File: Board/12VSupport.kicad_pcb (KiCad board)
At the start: 2 copper layers, 106.7 x 123.2 mm, 86 parts, among them J1 12V, J2 BATT, J3 BUCK_IN, J4 BUCK_OUT, J5 BOOST_IN, J6 BOOST_OUT, J7 TMP36GZ, J8 HEATER, J9 ICSP, K1 SLA-05VDC-SL-C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

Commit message: Minor improvements
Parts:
- added C10: 100n, Capacitor_SMD:C_0805_2012Metric, F.Cu at (76.2, 50.8)
- U2: value PIC18F2480 -> PIC18F2480-ISO
- moved R23 2.37 mm to (131.8, 114.7)
- moved L3 0.40 mm to (130.2, 110.1)
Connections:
- F1 pad 2: Net-(F1-Pad2) -> B-
- K1 pad 11A: Net-(F1-Pad2) -> B-
- K1 pad 11B: Net-(F1-Pad2) -> B-
- K2 pad 11A: Net-(K2-Pad11A) -> B+
- K2 pad 11B: Net-(K2-Pad11A) -> B+
- R17 pad 1: BUCK+ -> B+
- R8 pad 1: BUCK- -> B-
- U4 pad 3: Net-(K2-Pad11A) -> B+
- U4 pad 4: Net-(K2-Pad11A) -> B+
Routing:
- net B+: track 0.00 -> 136.3 mm, vias 0 -> 6
- net Net-(K2-Pad11A): track 112.5 -> 0.00 mm, vias 6 -> 0
- net BUCK+: track 166.2 -> 74.9 mm, vias 2 -> 1
- net B-: track 0.00 -> 70.1 mm
- net Net-(F1-Pad2): track 58.3 -> 0.00 mm
- net BUCK-: track 109.5 -> 52.3 mm, vias 1 -> 0
- net GND: track 493.5 -> 439.1 mm, vias 53 -> 50
- net CURR_SENSE: track 135.0 -> 131.7 mm, vias 4 -> 2
- net Net-(J1-Pin_2): track 18.4 -> 16.2 mm
- net VCC: track 317.0 -> 315.1 mm
- net /MCU/VPP: track 21.6 -> 19.7 mm
- net Net-(J7-Pin_2): track 61.4 -> 62.5 mm
- net Net-(U5A--): track 21.4 -> 20.5 mm
- net REL_HEATER: track 158.4 -> 159.2 mm
- net /MCU/VCC_PIC: track 50.5 -> 49.6 mm
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
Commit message: Rev. 1.1
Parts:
- moved J8 0.47 mm to (48.5, 77.6)
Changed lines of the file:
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@@
 	(footprint "TerminalBlock:TerminalBlock_Altech_AK300-2_P5.00mm"
 		(layer "F.Cu")
-		(at 48.4105 77.136 90)
+		(at 48.514 77.597 90)
 		(descr "Altech AK300 terminal block, pitch 5.0mm, 45 degree angled, see http://www.mouser.com/ds/2/16/PCBMETRC-24178.pdf")
 		(tags "Altech AK300 terminal block pitch 5.0mm")
@@
 	)
 	(segment
-		(start 58.674 67.564)
-		(end 54.102 72.136)
-		(width 1.2)
+		(start 101.098167 49.917167)
+		(end 104.919 53.738)
+		(width 0.4)
 		(layer "F.Cu")
 		(net 3)
 	)
 	(segment
-		(start 101.098167 49.917167)
-		(end 104.919 53.738)
-		(width 0.4)
+		(start 104.14 67.564)
+		(end 58.674 67.564)
+		(width 1.2)
 		(layer "F.Cu")
 		(net 3)
@@
 	)
 	(segment
+		(start 106.172 69.596)
+		(end 104.14 67.564)
+		(width 1.2)
+		(layer "F.Cu")
+		(net 3)
+	)
+	(segment
+		(start 48.975 72.136)
+		(end 48.514 72.597)
+		(width 1.2)
+		(layer "F.Cu")
+		(net 3)
+	)
+	(segment
 		(start 131.185 65.193)
 		(end 126.493 65.193)
@@
 	)
 	(segment
+		(start 58.674 67.564)
+		(end 54.102 72.136)
+		(width 1.2)
+		(layer "F.Cu")
+		(net 3)
+	)
+	(segment
 		(start 93.726 54.864)
 		(end 95.28 56.418)
@@
 	)
 	(segment
+		(start 54.102 72.136)
+		(end 48.975 72.136)
+		(width 1.2)
+		(layer "F.Cu")
+		(net 3)
+	)
+	(segment
 		(start 104.919 53.738)
 		(end 116.078 53.738)
@@
 	)
 	(segment
-		(start 54.102 72.136)
-		(end 48.4105 72.136)
-		(width 1.2)
-		(layer "F.Cu")
-		(net 3)
-	)
-	(segment
 		(start 57.1405 113.886)
 		(end 65.118 113.886)
@@
 	)
 	(segment
-		(start 58.674 67.564)
-		(end 104.14 67.564)
-		(width 1.2)
-		(layer "F.Cu")
-		(net 3)
-	)
-	(segment
-		(start 104.14 67.564)
-		(end 106.172 69.596)
-		(width 1.2)
-		(layer "F.Cu")
-		(net 3)
-	)
-	(segment
 		(start 106.172 72.136)
 		(end 106.172 69.596)
@@
 	)
 	(segment
-		(start 61.5655 77.464)
-		(end 48.7385 77.464)
+		(start 48.647 77.464)
+		(end 48.514 77.597)
 		(width 1.2)
 		(layer "F.Cu")
@@
 	)
 	(segment
-		(start 48.7385 77.464)
-		(end 48.4105 77.136)
+		(start 61.5655 77.464)
+		(end 48.647 77.464)
 		(width 1.2)
 		(layer "F.Cu")

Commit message: Silkscreen fix
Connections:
- net Net-(J6-Pin_1) renamed /BO-
- net Net-(J6-Pin_2) renamed /BO+
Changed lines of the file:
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@@
 	(net 27 "/BUCK_OUT+")
 	(net 28 "/BOOST_IN+")
-	(net 29 "Net-(J6-Pin_1)")
-	(net 30 "Net-(J6-Pin_2)")
+	(net 29 "/BO+")
+	(net 30 "/BO-")
 	(net 31 "Net-(J8-Pin_1)")
 	(net 32 "/MCU/VPP")
@@
 			(layers "*.Cu" "*.Mask" "F.SilkS")
 			(remove_unused_layers no)
-			(net 29 "Net-(J6-Pin_1)")
+			(net 30 "/BO-")
 			(pinfunction "Pin_1")
 			(pintype "passive")
@@
 			(layers "*.Cu" "*.Mask" "F.SilkS")
 			(remove_unused_layers no)
-			(net 30 "Net-(J6-Pin_2)")
+			(net 29 "/BO+")
 			(pinfunction "Pin_2")
 			(pintype "passive")
@@
 			(layers "*.Cu" "*.Mask")
 			(remove_unused_layers no)
-			(net 30 "Net-(J6-Pin_2)")
+			(net 29 "/BO+")
 			(pintype "passive")
 		)
@@
 			(layers "*.Cu" "*.Mask")
 			(remove_unused_layers no)
-			(net 29 "Net-(J6-Pin_1)")
+			(net 30 "/BO-")
 			(pintype "passive")
 		)
@@
 	)
 	(gr_text "+"
-		(at 56.896 148.336 270)
+		(at 44.196 148.336 270)
 		(layer "F.SilkS")
 		(effects
@@
 	)
 	(gr_text "+"
-		(at 91.948 148.336 270)
+		(at 79.248 148.336 270)
 		(layer "F.SilkS")
 		(effects
@@
 	)
 	(gr_text "+"
-		(at 74.168 148.336 270)
+		(at 61.468 148.336 270)
 		(layer "F.SilkS")
 		(effects
@@
 	)
 	(gr_text "+"
-		(at 109.728 148.336 270)
+		(at 97.028 148.336 270)
 		(layer "F.SilkS")
 		(effects
@@
 	)
 	(segment
-		(start 63.945 109.304)
-		(end 63.945 122.618)
-		(width 2.4)
-		(layer "B.Cu")
-		(net 29)
-	)
-	(segment
-		(start 63.945 122.618)
-		(end 60.452 126.111)
-		(width 2.4)
-		(layer "B.Cu")
-		(net 29)
-	)
-	(segment
-		(start 60.452 126.111)
-		(end 60.452 141.288)
-		(width 2.4)
-		(layer "B.Cu")
-		(net 29)
-	)
-	(segment
-		(start 63.627 108.986)
-		(end 63.945 109.304)
-		(width 2.4)
-		(layer "B.Cu")
-		(net 29)
-	)
-	(segment
-		(start 60.452 141.288)
-		(end 72.644 153.48)
-		(width 2.4)
-		(layer "B.Cu")
-		(net 29)
-	)
-	(segment
 		(start 99.29 110.998)
 		(end 101.558 108.73)
 		(width 2.4)
 		(layer "F.Cu")
-		(net 30)
+		(net 29)
 	)
 	(segment
@@
 		(width 2.4)
 		(layer "F.Cu")
-		(net 30)
+		(net 29)
 	)
 	(segment
@@
 		(width 2.4)
 		(layer "F.Cu")
-		(net 30)
+		(net 29)
 	)
 	(segment
@@
 		(width 2.4)
 		(layer "F.Cu")
-		(net 30)
+		(net 29)
 	)
 	(segment
@@
 		(width 2.4)
 		(layer "F.Cu")
-		(net 30)
+		(net 29)
 	)
 	(via
@@
 		(drill 0.8)
 		(layers "F.Cu" "B.Cu")
-		(net 30)
+		(net 29)
 	)
 	(segment
@@
 		(width 2.4)
 		(layer "B.Cu")
-		(net 30)
+		(net 29)
 	)
 	(segment
@@
 		(width 2.4)
 		(layer "B.Cu")
-		(net 30)
+		(net 29)
 	)
 	(segment
@@
 		(width 2.4)
 		(layer "B.Cu")
-		(net 30)
+		(net 29)
 	)
 	(segment
@@
 		(width 2.4)
 		(layer "B.Cu")
+		(net 29)
+	)
+	(segment
+		(start 63.945 109.304)
+		(end 63.945 122.618)
+		(width 2.4)
+		(layer "B.Cu")
+		(net 30)
+	)
+	(segment
+		(start 63.945 122.618)
+		(end 60.452 126.111)
+		(width 2.4)
+		(layer "B.Cu")
+		(net 30)
+	)
+	(segment
+		(start 60.452 126.111)
+		(end 60.452 141.288)
+		(width 2.4)
+		(layer "B.Cu")
+		(net 30)
+	)
+	(segment
+		(start 63.627 108.986)
+		(end 63.945 109.304)
+		(width 2.4)
+		(layer "B.Cu")
+		(net 30)
+	)
+	(segment
+		(start 60.452 141.288)
+		(end 72.644 153.48)
+		(width 2.4)
+		(layer "B.Cu")

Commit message: Bugfixes
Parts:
- added R20: 33K, Resistor_SMD:R_0805_2012Metric, F.Cu at (58.2, 65.3)
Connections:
- C6 pad 1: Net-(U5C--) -> Net-(U5C-+)
- R5 pad 2: Net-(U5C--) -> Net-(U5C-+)
- R6 pad 1: Net-(U5C--) -> Net-(U5C-+)
- U5 pad 10: 12V_SENSE -> Net-(U5C-+)
- U5 pad 9: Net-(U5C--) -> 12V_SENSE
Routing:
- net Net-(U5C-+): track 0.00 -> 18.8 mm
- net Net-(U5C--): track 18.3 -> 0.00 mm
- net GND: track 439.1 -> 442.7 mm
- net 12V_SENSE: track 106.6 -> 103.1 mm
- net +12V: track 312.9 -> 311.2 mm

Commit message: Bugfixes
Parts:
- D6: value RED -> DCHG
- D7: value GREEN -> CHG
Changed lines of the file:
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@@
 			)
 		)
-		(property "Value" "GREEN"
+		(property "Value" "CHG"
 			(at 0 1.65 90)
 			(layer "F.Fab")
@@
 			)
 		)
-		(property "Value" "RED"
+		(property "Value" "DCHG"
 			(at 0 1.65 90)
 			(layer "F.Fab")

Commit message: Set version number to 1.2. Various fixes. Add fan connector.
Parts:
- added J10: FAN, Connector_JST:JST_PH_B2B-PH-K_1x02_P2.00mm_Vertical, F.Cu at (142.4, 110.1)
- added Q7: IRLML2502, Package_TO_SOT_SMD:SOT-23, F.Cu at (137.2, 113.2)
- added R21: 1, Resistor_SMD:R_2512_6332Metric, F.Cu at (48.8, 114.8)
- Q1, Q2: value BSS138 -> IRLML2502
- Q3: value MMBF170 -> IRLML2502
- moved Q5 41.6 mm to (70.2, 79.5), turned to 0 degrees
- moved Q6 38.3 mm to (78.5, 77.3), turned to 90 degrees
- moved R24 36.9 mm to (62.0, 78.0), turned to -90 degrees
- moved D2 10.3 mm to (79.1, 84.5), turned to 180 degrees
- moved Q2 9.19 mm to (81.7, 115.6)
- moved L3 6.93 mm to (123.4, 111.8)
- moved C12 6.23 mm to (130.3, 109.6)
- moved R23 6.05 mm to (125.9, 115.7)
- moved L2 5.64 mm to (115.8, 62.7)
- moved Q4 5.12 mm to (70.2, 71.5)
- moved D15 2.17 mm to (142.1, 100.2)
- moved REF** 2.03 mm to (89.9, 67.7)
- moved REF** 2.03 mm to (104.1, 67.2)
- moved C1 1.78 mm to (122.7, 102.9)
- moved R20 0.51 mm to (58.7, 65.3)
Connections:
- C2 pad 1: Net-(D14-K) -> VDD
- C5 pad 1: Net-(D14-K) -> VDD
- D14 pad 1: Net-(D14-K) -> VDD
- D5 pad 1: Net-(D14-K) -> VDD
- L2 pad 2: +12V -> VDD
- Q5 pad 2: /BOOST_IN+ -> Net-(Q5-D)
- U1 pad 1: Net-(D14-K) -> VDD
- U2 pad 26: unconnected-(U2-RB5/KBI1/PGM-Pad26) -> /MCU/FAN
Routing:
- net Net-(Q5-D): track 0.00 -> 51.4 mm, vias 0 -> 2
- net VDD: track 0.00 -> 50.4 mm, vias 0 -> 2
- net Net-(D14-K): track 36.0 -> 0.00 mm
- net EN_BOOST_IN: track 70.0 -> 104.9 mm, vias 2 -> 4
- net VCC: track 315.1 -> 328.1 mm
- net /MCU/FAN: track 0.00 -> 11.6 mm, vias 0 -> 2
- net Net-(Q5-G): track 28.3 -> 17.1 mm
- net REL_BOOST_IN: track 83.6 -> 94.4 mm
- net Net-(D3-A): track 62.5 -> 70.3 mm
- net Net-(J10-Pin_2): track 0.00 -> 7.40 mm
- net +12V: track 311.2 -> 304.2 mm, vias 4 -> 3
- net GND: track 442.7 -> 435.9 mm, vias 50 -> 49
- net /Sensors/V+_OP: track 46.8 -> 41.1 mm
- net Net-(J8-Pin_1): track 13.1 -> 18.4 mm
- net /MCU/VPP: track 19.7 -> 23.7 mm
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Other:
- board text added: "2x IRLM2502"
- board text added: "Rev. 1.2 2025"
- board text removed: "Rev. 1.1 2024-2025"

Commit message: Adds connector for external duo LED
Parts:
- added J11: DUO LED, Connector_JST:JST_PH_B3B-PH-K_1x03_P2.00mm_Vertical, F.Cu at (142.4, 140.3)
- added R22: 470, Resistor_SMD:R_0805_2012Metric, F.Cu at (142.1, 145.4)
- added R25: 470, Resistor_SMD:R_0805_2012Metric, F.Cu at (138.7, 145.5)
- R12: value 470 -> 5x470
- moved R11 21.0 mm to (116.0, 143.6)
- moved D6 18.7 mm to (124.3, 143.7)
- moved D8 18.7 mm to (118.7, 143.6)
- moved D7 18.7 mm to (121.5, 143.6)
- moved R10 17.5 mm to (122.4, 140.1), turned to 180 degrees
- moved R9 15.7 mm to (127.0, 140.1), turned to 180 degrees
- moved R12 1.78 mm to (118.6, 153.4)
- moved R13 1.63 mm to (121.5, 153.3)
- moved R14 1.63 mm to (124.5, 153.3)
- moved R15 1.63 mm to (127.4, 153.3)
- moved R16 1.63 mm to (130.3, 153.3)
- moved D10 0.92 mm to (121.5, 157.6)
- moved D11 0.92 mm to (124.5, 157.6)
- moved D12 0.92 mm to (127.4, 157.6)
- moved D13 0.92 mm to (130.3, 157.6)
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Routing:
- net Net-(U2-RX/DT/RC7): track 12.6 -> 33.6 mm, vias 0 -> 2
- net Net-(U2-TX/CK/RC6): track 15.8 -> 30.2 mm
- net Net-(J11-Pin_3): track 0.00 -> 11.2 mm
- net REL_HEATER: track 158.8 -> 148.9 mm
- net GND: track 435.9 -> 445.8 mm
- net Net-(J11-Pin_1): track 0.00 -> 7.68 mm
- net Net-(U2-RB4/KBI0/AN9): track 30.9 -> 32.6 mm
- net Net-(U2-RB2/AN8/INT2/CANTX): track 34.3 -> 35.7 mm
- net Net-(U2-RB0/INT0/AN10): track 36.9 -> 37.9 mm
- net Net-(D9-A): track 3.13 -> 2.26 mm
- net Net-(U2-RB3/CANRX): track 32.4 -> 33.3 mm
- net Net-(U2-RB1/INT1/AN8): track 35.9 -> 36.7 mm
- net Net-(D13-A): track 3.10 -> 2.39 mm
- net Net-(D12-A): track 3.10 -> 2.39 mm
- net Net-(D11-A): track 3.10 -> 2.39 mm
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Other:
- board text added: "5x470"
- board text added: "C"
- board text added: "D"

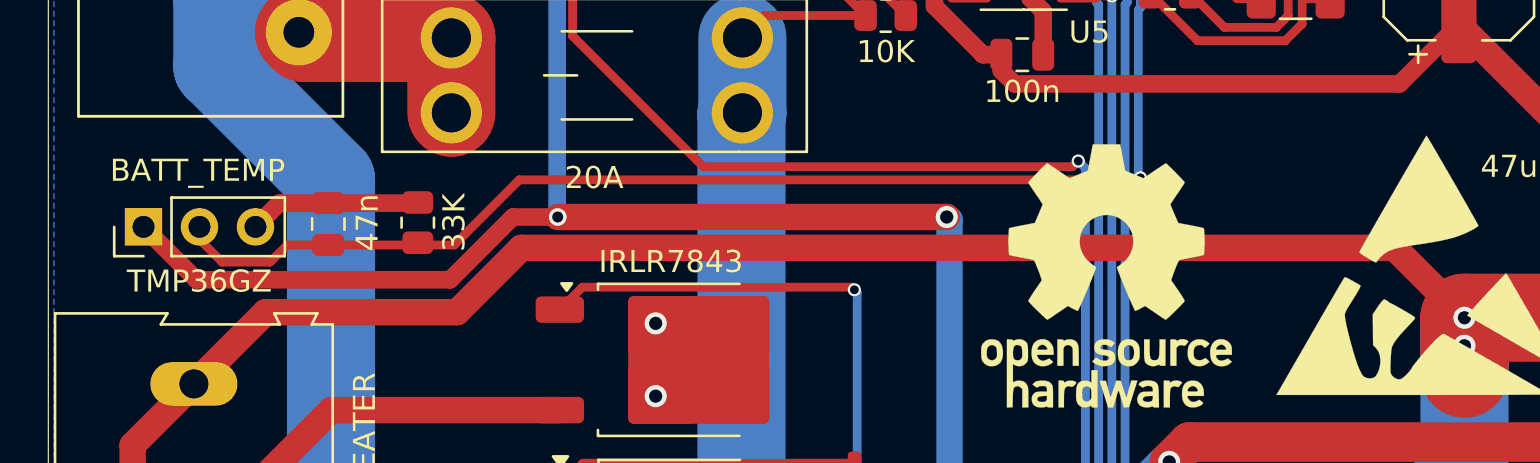
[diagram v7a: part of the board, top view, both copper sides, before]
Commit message: Changed battery temp sensor connector.
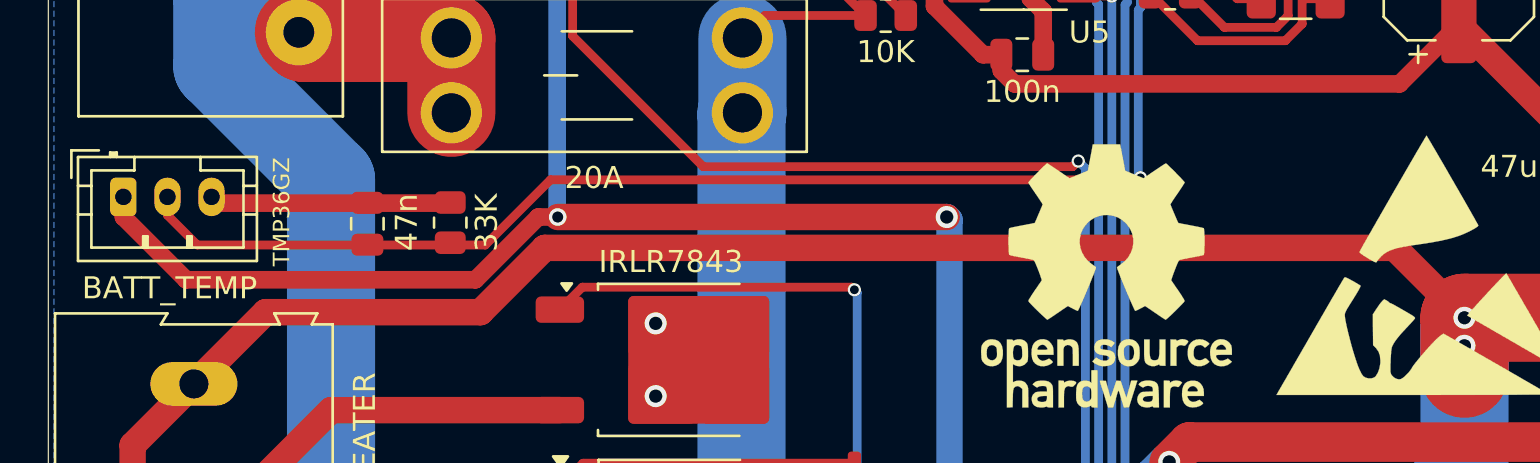
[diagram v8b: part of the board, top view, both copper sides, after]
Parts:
- J7: footprint Connector_PinHeader_2.54mm:PinHeader_1x03_P2.54mm_Vertical -> Connector_JST:JST_PH_B3B-PH-K_1x03_P2.00mm_Vertical
- R12: value 5x470 -> 470
- moved C7 1.78 mm to (56.4, 65.3)
- moved J7 1.64 mm to (45.3, 64.1), turned to 0 degrees
- moved R20 1.47 mm to (60.1, 65.3)
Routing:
- net GND: track 445.8 -> 449.0 mm
- net VCC: track 328.1 -> 330.1 mm
- net Net-(J7-Pin_2): track 62.0 -> 63.6 mm
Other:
- board text added: "TMP36GZ"
